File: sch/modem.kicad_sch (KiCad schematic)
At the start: 46 parts, among them J10 TestPoint, J11 TestPoint, J12 TestPoint, J13 TestPoint, J14 TestPoint, J4 CONMHF1-SMD-G-T, J5 CONMHF1-SMD-G-T, J6 TestPoint, J7 TestPoint, J8 TestPoint, J9 TestPoint, P1 SF72S006VBAR2500, U1 RC7620_1104625, U2 NX3008NBKW_115, U3 NX3008NBKW_115, U4 NX3008NBKW_115, U5 NX3008NBKW_115, U6 NX3008NBKW_115, U7 NX3008NBKW_115

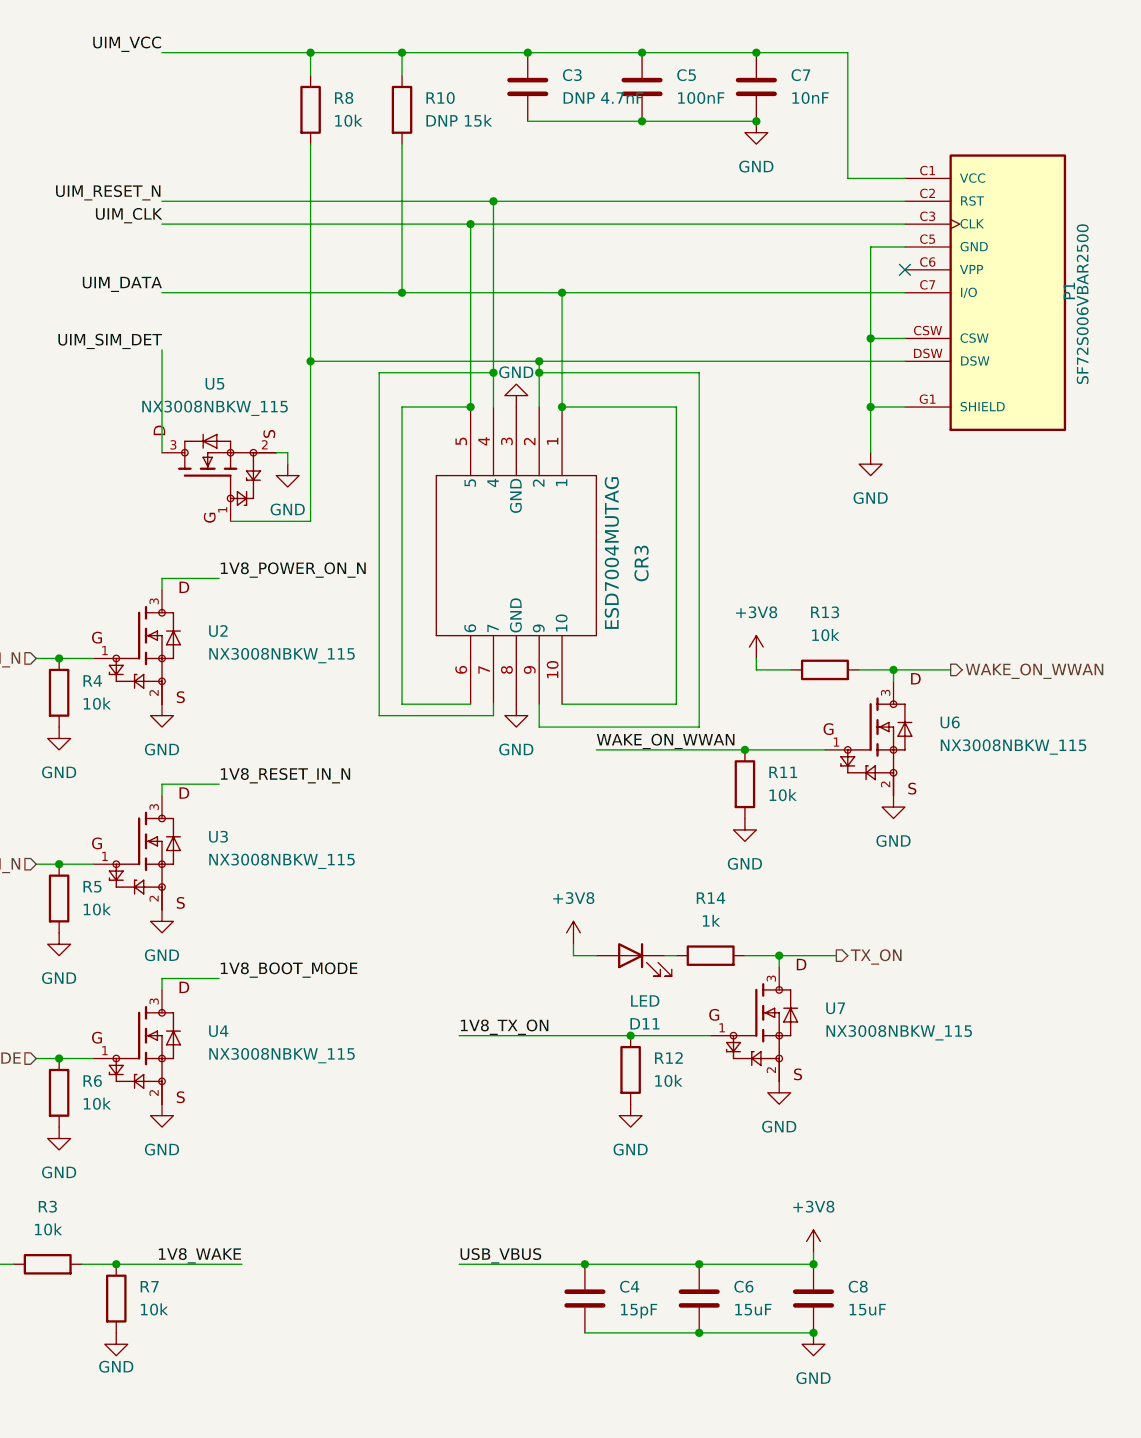
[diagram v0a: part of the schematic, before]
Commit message: added ports to powersupply
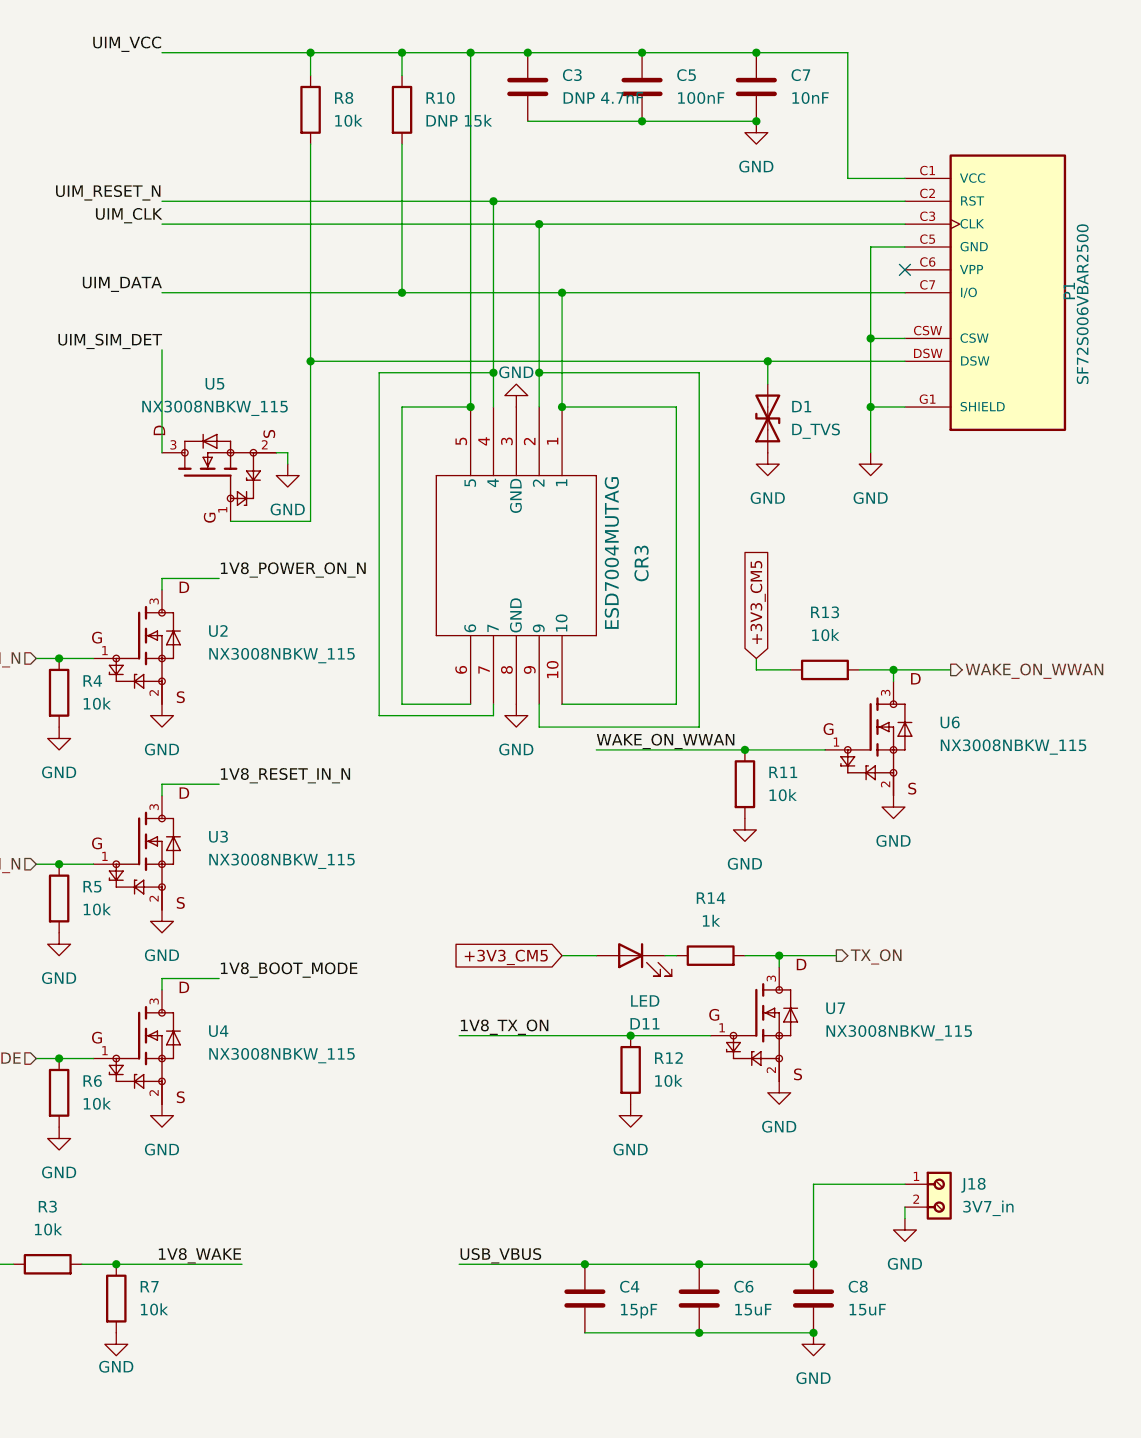
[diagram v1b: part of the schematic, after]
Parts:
- added D1: D_TVS, Diode_SMD:D_0402_1005Metric, symbol Device:D_TVS
- added J18: 3V7_in, 691137710002:691137710002, symbol 691137710002:691137710002
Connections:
- net GND: now also D1.1 (A1), J18.2
- net UIM_CLK: now also CR3.2, CR3.9; no longer CR3.5, CR3.6
- net UIM_VCC: now also CR3.5, CR3.6
- net at P1.DSW, R8.2, U5.1: now also D1.2 (A2); no longer CR3.2, CR3.9
- net +3V8 renamed VBAT_BB
- net VBAT_BB: now also J18.1; no longer D11.2 (A), R13.1
- new net +3V3_CM5: D11.2 (A), R13.1

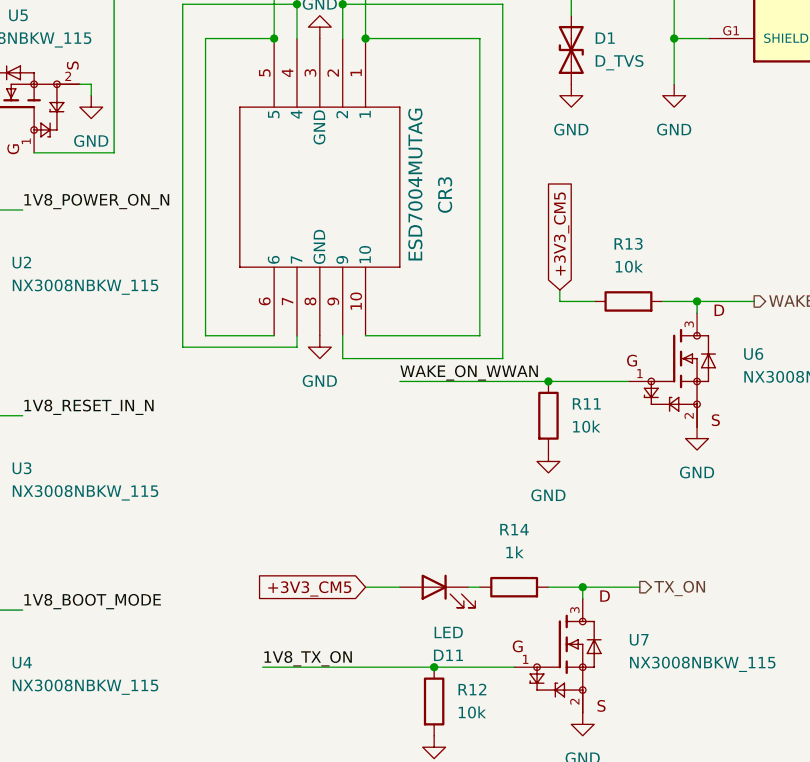
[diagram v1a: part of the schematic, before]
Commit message: fix annotation and clean up schematics
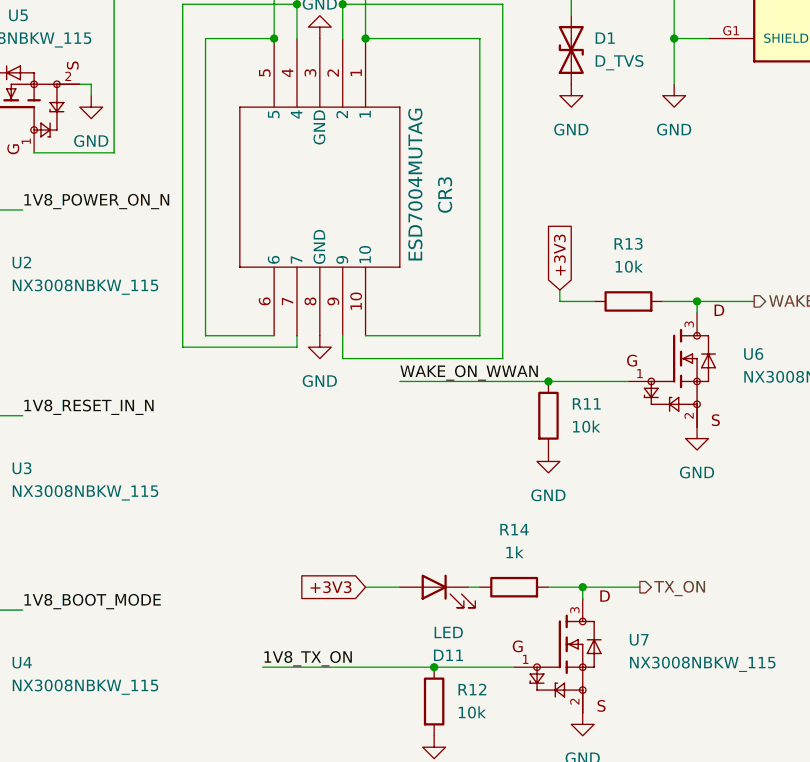
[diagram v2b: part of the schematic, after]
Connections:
- net +3V3_CM5 renamed +3V3
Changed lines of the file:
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@@
 	(title_block
 		(title "Modem")
-		(date "2026-01-29")
+		(date "2026-02-13")
 		(rev "0")
 		(company "NTNU, NINA")
@@
 		)
 	)
-	(global_label "+3V3_CM5"
+	(global_label "+3V3"
 		(shape input)
 		(at 223.52 116.84 180)
@@
 		)
 	)
-	(global_label "+3V3_CM5"
+	(global_label "+3V3"
 		(shape input)
 		(at 245.11 83.82 90)

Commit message: work pcb about 70 percent
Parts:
- J10, J11, J12, J13, J14, J6, J7, J8, J9, TP1, TP3, TP4, TP5, TP6: footprint TestPoint:TestPoint_Loop_D2.50mm_Drill1.85mm -> TestPoint:TestPoint_Loop_D2.60mm_Drill1.6mm_Beaded
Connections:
- net WAKE_ON_WWAN: no longer R13.2, U6.3
- new net WAKE_ON_WWAN_port: R13.2, U6.3
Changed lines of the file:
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@@
 	)
 	(label "USB_VBUS"
-		(at 212.09 151.13 0)
+		(at 212.09 151.13 180)
 		(effects
 			(font
 				(size 1.27 1.27)
 			)
-			(justify left bottom)
+			(justify right bottom)
 		)
 	)
@@
 		)
 	)
-	(hierarchical_label "WAKE_ON_WWAN"
+	(hierarchical_label "WAKE_ON_WWAN_port"
 		(shape output)
 		(at 266.7 85.09 0)
@@
 			)
 		)
-		(property "Footprint" "TestPoint:TestPoint_Loop_D2.50mm_Drill1.85mm"
+		(property "Footprint" "TestPoint:TestPoint_Loop_D2.60mm_Drill1.6mm_Beaded"
 			(at 44.45 44.45 0)
 			(effects
@@
 			)
 		)
-		(property "Footprint" "TestPoint:TestPoint_Loop_D2.50mm_Drill1.85mm"
+		(property "Footprint" "TestPoint:TestPoint_Loop_D2.60mm_Drill1.6mm_Beaded"
 			(at 125.73 125.73 0)
 			(effects
@@
 			)
 		)
-		(property "Footprint" "TestPoint:TestPoint_Loop_D2.50mm_Drill1.85mm"
+		(property "Footprint" "TestPoint:TestPoint_Loop_D2.60mm_Drill1.6mm_Beaded"
 			(at 125.73 64.77 0)
 			(effects
@@
 			)
 		)
-		(property "Footprint" "TestPoint:TestPoint_Loop_D2.50mm_Drill1.85mm"
+		(property "Footprint" "TestPoint:TestPoint_Loop_D2.60mm_Drill1.6mm_Beaded"
 			(at 125.73 123.19 0)
 			(effects
@@
 			)
 		)
-		(property "Footprint" "TestPoint:TestPoint_Loop_D2.50mm_Drill1.85mm"
+		(property "Footprint" "TestPoint:TestPoint_Loop_D2.60mm_Drill1.6mm_Beaded"
 			(at 125.73 120.65 0)
 			(effects
@@
 			)
 		)
-		(property "Footprint" "TestPoint:TestPoint_Loop_D2.50mm_Drill1.85mm"
+		(property "Footprint" "TestPoint:TestPoint_Loop_D2.60mm_Drill1.6mm_Beaded"
 			(at 125.73 118.11 0)
 			(effects
@@
 			)
 		)
-		(property "Footprint" "TestPoint:TestPoint_Loop_D2.50mm_Drill1.85mm"
+		(property "Footprint" "TestPoint:TestPoint_Loop_D2.60mm_Drill1.6mm_Beaded"
 			(at 125.73 115.57 0)
 			(effects
@@
 			)
 		)
-		(property "Footprint" "TestPoint:TestPoint_Loop_D2.50mm_Drill1.85mm"
+		(property "Footprint" "TestPoint:TestPoint_Loop_D2.60mm_Drill1.6mm_Beaded"
 			(at 125.73 128.27 0)
 			(effects
@@
 			)
 		)
-		(property "Footprint" "TestPoint:TestPoint_Loop_D2.50mm_Drill1.85mm"
+		(property "Footprint" "TestPoint:TestPoint_Loop_D2.60mm_Drill1.6mm_Beaded"
 			(at 125.73 110.49 0)
 			(effects
@@
 			)
 		)
-		(property "Footprint" "TestPoint:TestPoint_Loop_D2.50mm_Drill1.85mm"
+		(property "Footprint" "TestPoint:TestPoint_Loop_D2.60mm_Drill1.6mm_Beaded"
 			(at 44.45 46.99 0)
 			(effects
@@
 			)
 		)
-		(property "Footprint" "TestPoint:TestPoint_Loop_D2.50mm_Drill1.85mm"
+		(property "Footprint" "TestPoint:TestPoint_Loop_D2.60mm_Drill1.6mm_Beaded"
 			(at 44.45 39.37 0)
 			(effects
@@
 			)
 		)
+		(property "Field5" ""
+			(at 44.45 44.45 90)
+			(effects
+				(font
+					(size 1.27 1.27)
+				)
+				(hide yes)
+			)
+		)
 		(pin "1"
 		)
@@
 			)
 		)
-		(property "Footprint" "TestPoint:TestPoint_Loop_D2.50mm_Drill1.85mm"
+		(property "Footprint" "TestPoint:TestPoint_Loop_D2.60mm_Drill1.6mm_Beaded"
 			(at 125.73 113.03 0)
 			(effects
@@
 			)
 		)
-		(property "Footprint" "TestPoint:TestPoint_Loop_D2.50mm_Drill1.85mm"
+		(property "Footprint" "TestPoint:TestPoint_Loop_D2.60mm_Drill1.6mm_Beaded"
 			(at 125.73 62.23 0)
 			(effects
@@
 			)
 		)
-		(property "Footprint" "TestPoint:TestPoint_Loop_D2.50mm_Drill1.85mm"
+		(property "Footprint" "TestPoint:TestPoint_Loop_D2.60mm_Drill1.6mm_Beaded"
 			(at 125.73 107.95 0)
 			(effects

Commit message: more pcb
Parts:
- J10, J11, J12, J13, J14, J6, J7, J8, J9, TP1, TP3, TP4: footprint TestPoint:TestPoint_Loop_D2.60mm_Drill1.6mm_Beaded -> TestPoint:TestPoint_Loop_D2.50mm_Drill1.0mm
- TP2: footprint TestPoint:TestPoint_Loop_D2.50mm_Drill1.85mm -> TestPoint:TestPoint_Loop_D2.50mm_Drill1.0mm
- TP5, TP6: footprint TestPoint:TestPoint_Loop_D2.60mm_Drill1.6mm_Beaded -> TestPoint:TestPoint_Pad_D1.5mm
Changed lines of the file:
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@@
 			)
 		)
-		(property "Footprint" "TestPoint:TestPoint_Loop_D2.50mm_Drill1.85mm"
+		(property "Footprint" "TestPoint:TestPoint_Loop_D2.50mm_Drill1.0mm"
 			(at 44.45 41.91 0)
 			(effects
@@
 			)
 		)
-		(property "Footprint" "TestPoint:TestPoint_Loop_D2.60mm_Drill1.6mm_Beaded"
+		(property "Footprint" "TestPoint:TestPoint_Loop_D2.50mm_Drill1.0mm"
 			(at 44.45 44.45 0)
 			(effects
@@
 			)
 		)
-		(property "Footprint" "TestPoint:TestPoint_Loop_D2.60mm_Drill1.6mm_Beaded"
+		(property "Footprint" "TestPoint:TestPoint_Loop_D2.50mm_Drill1.0mm"
 			(at 125.73 125.73 0)
 			(effects
@@
 			)
 		)
-		(property "Footprint" "TestPoint:TestPoint_Loop_D2.60mm_Drill1.6mm_Beaded"
+		(property "Footprint" "TestPoint:TestPoint_Pad_D1.5mm"
 			(at 125.73 64.77 0)
 			(effects
@@
 			)
 		)
-		(property "Footprint" "TestPoint:TestPoint_Loop_D2.60mm_Drill1.6mm_Beaded"
+		(property "Footprint" "TestPoint:TestPoint_Loop_D2.50mm_Drill1.0mm"
 			(at 125.73 123.19 0)
 			(effects
@@
 			)
 		)
-		(property "Footprint" "TestPoint:TestPoint_Loop_D2.60mm_Drill1.6mm_Beaded"
+		(property "Footprint" "TestPoint:TestPoint_Loop_D2.50mm_Drill1.0mm"
 			(at 125.73 120.65 0)
 			(effects
@@
 			)
 		)
-		(property "Footprint" "TestPoint:TestPoint_Loop_D2.60mm_Drill1.6mm_Beaded"
+		(property "Footprint" "TestPoint:TestPoint_Loop_D2.50mm_Drill1.0mm"
 			(at 125.73 118.11 0)
 			(effects
@@
 			)
 		)
-		(property "Footprint" "TestPoint:TestPoint_Loop_D2.60mm_Drill1.6mm_Beaded"
+		(property "Footprint" "TestPoint:TestPoint_Loop_D2.50mm_Drill1.0mm"
 			(at 125.73 115.57 0)
 			(effects
@@
 			)
 		)
-		(property "Footprint" "TestPoint:TestPoint_Loop_D2.60mm_Drill1.6mm_Beaded"
+		(property "Footprint" "TestPoint:TestPoint_Loop_D2.50mm_Drill1.0mm"
 			(at 125.73 128.27 0)
 			(effects
@@
 			)
 		)
-		(property "Footprint" "TestPoint:TestPoint_Loop_D2.60mm_Drill1.6mm_Beaded"
+		(property "Footprint" "TestPoint:TestPoint_Loop_D2.50mm_Drill1.0mm"
 			(at 125.73 110.49 0)
 			(effects
@@
 			)
 		)
-		(property "Footprint" "TestPoint:TestPoint_Loop_D2.60mm_Drill1.6mm_Beaded"
+		(property "Footprint" "TestPoint:TestPoint_Loop_D2.50mm_Drill1.0mm"
 			(at 44.45 46.99 0)
 			(effects
@@
 			)
 		)
-		(property "Footprint" "TestPoint:TestPoint_Loop_D2.60mm_Drill1.6mm_Beaded"
+		(property "Footprint" "TestPoint:TestPoint_Loop_D2.50mm_Drill1.0mm"
 			(at 44.45 39.37 0)
 			(effects
@@
 			)
 		)
-		(property "Footprint" "TestPoint:TestPoint_Loop_D2.60mm_Drill1.6mm_Beaded"
+		(property "Footprint" "TestPoint:TestPoint_Loop_D2.50mm_Drill1.0mm"
 			(at 125.73 113.03 0)
 			(effects
@@
 			)
 		)
-		(property "Footprint" "TestPoint:TestPoint_Loop_D2.60mm_Drill1.6mm_Beaded"
+		(property "Footprint" "TestPoint:TestPoint_Pad_D1.5mm"
 			(at 125.73 62.23 0)
 			(effects
@@
 			)
 		)
-		(property "Footprint" "TestPoint:TestPoint_Loop_D2.60mm_Drill1.6mm_Beaded"
+		(property "Footprint" "TestPoint:TestPoint_Loop_D2.50mm_Drill1.0mm"
 			(at 125.73 107.95 0)
 			(effects

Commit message: mjeu
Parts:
- removed J4, J5: CONMHF1-SMD-G-T, CONMHF1-SMD-G-T:LINX_CONMHF1-SMD-G-T, symbol CONMHF1-SMD-G-T:CONMHF1-SMD-G-T
- added J4, J5: EMPCB.SMAFSTJ.B.HT, EMPCB.SMAFSTJ.B.HT:TAOGLAS_EMPCB.SMAFSTJ.B.HT, symbol EMPCB.SMAFSTJ.B.HT:EMPCB.SMAFSTJ.B.HT
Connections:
- net GND: now also J4.SH1, J4.SH2, J4.SH3, J4.SH4, J5.SH1, J5.SH2, J5.SH3, J5.SH4
- net at D7.2 (A2), U1.31 (RF_DIV): now also J5.1
- net at D6.2 (A2), U1.49 (RF_MAIN): now also J4.1
